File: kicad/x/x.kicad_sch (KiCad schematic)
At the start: 4 parts

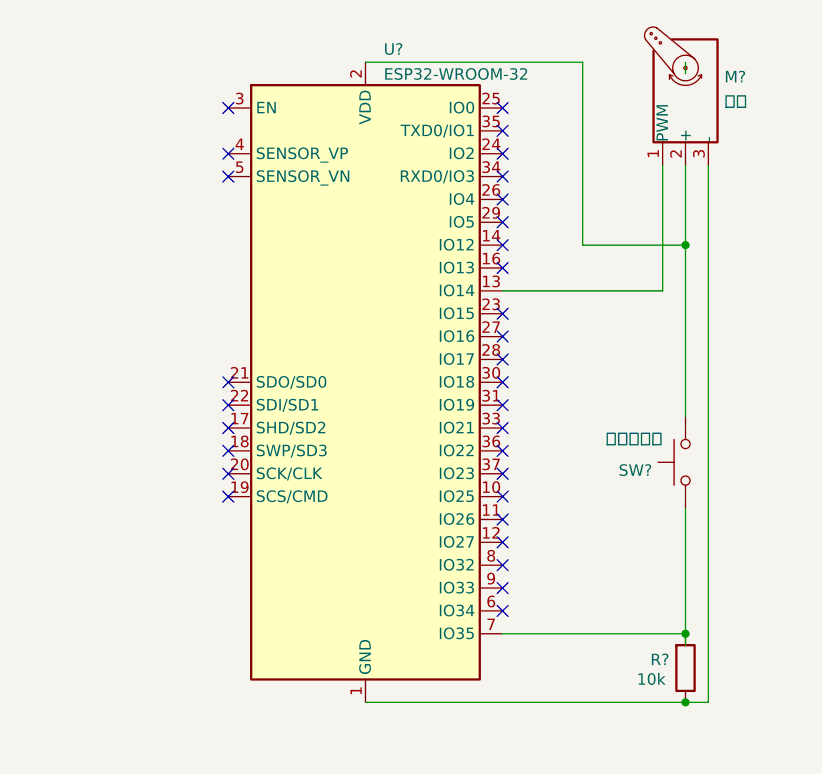
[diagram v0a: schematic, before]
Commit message: 电阻更新
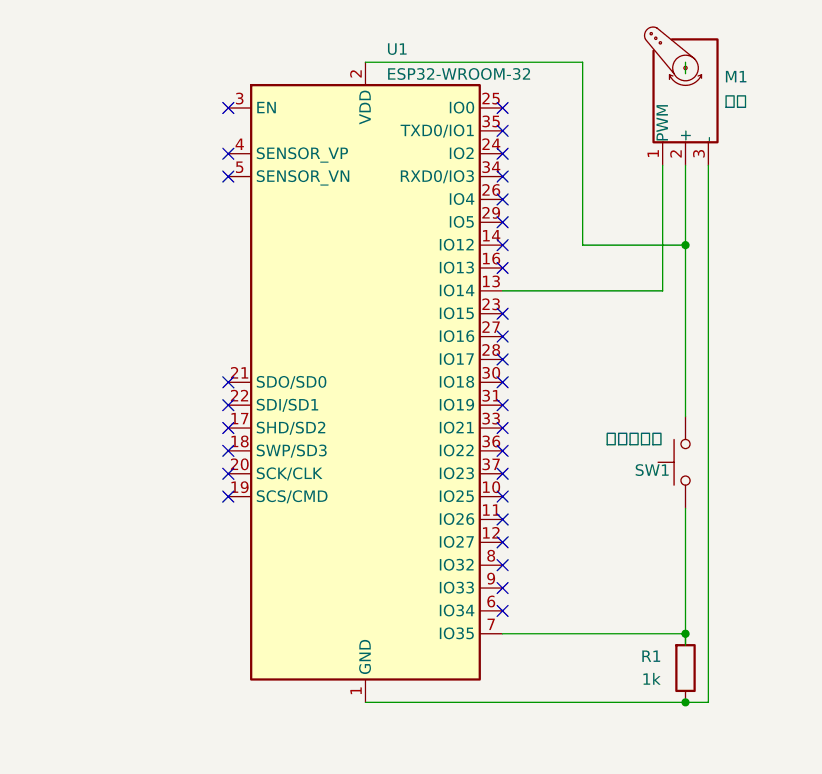
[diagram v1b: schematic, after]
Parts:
- R1: renamed from R?; value 10k -> 1k
- gave numbers to parts that had none: 3
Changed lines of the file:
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@@
   (symbol (lib_id "Motor:Motor_Servo") (at 165.1 24.13 90) (unit 1)
     (in_bom yes) (on_board yes) (fields_autoplaced)
-    (property "Reference" "M?" (id 0) (at 169.418 21.9626 90)
+    (property "Reference" "M1" (id 0) (at 169.418 21.9626 90)
       (effects (font (size 1.27 1.27)) (justify right))
     )
@@
   (symbol (lib_id "RF_Module:ESP32-WROOM-32") (at 129.54 55.88 0) (unit 1)
     (in_bom yes) (on_board yes) (fields_autoplaced)
-    (property "Reference" "U?" (id 0) (at 131.5594 18.8935 0)
+    (property "Reference" "U1" (id 0) (at 131.8832 18.8935 0)
       (effects (font (size 1.27 1.27)) (justify left))
     )
-    (property "Value" "ESP32-WROOM-32" (id 1) (at 131.5594 21.6686 0)
+    (property "Value" "ESP32-WROOM-32" (id 1) (at 131.8832 21.6686 0)
       (effects (font (size 1.27 1.27)) (justify left))
     )
@@
   (symbol (lib_id "Device:R") (at 165.1 87.63 0) (mirror x) (unit 1)
     (in_bom yes) (on_board yes)
-    (property "Reference" "R?" (id 0) (at 163.322 86.7215 0)
-      (effects (font (size 1.27 1.27)) (justify right))
-    )
-    (property "Value" "10k" (id 1) (at 161.29 88.9 0))
+    (property "Reference" "R1" (id 0) (at 161.29 86.36 0))
+    (property "Value" "1k" (id 1) (at 161.29 88.9 0))
     (property "Footprint" "" (id 2) (at 163.322 87.63 90)
       (effects (font (size 1.27 1.27)) hide)
@@
   (symbol (lib_id "Switch:SW_Push") (at 165.1 64.77 90) (unit 1)
     (in_bom yes) (on_board yes)
-    (property "Reference" "SW?" (id 0) (at 161.417 65.6785 90)
-      (effects (font (size 1.27 1.27)) (justify left))
-    )
+    (property "Reference" "SW1" (id 0) (at 161.417 65.6785 90))
     (property "Value" "雨滴传感器" (id 1) (at 162.56 62.23 90)
       (effects (font (size 1.27 1.27)) (justify left))
@@
   (symbol_instances
     (path "/3198b8ca-7d11-4e0c-89a4-c173f9fcf724"
-      (reference "M?") (unit 1) (value "舵机") (footprint "")
+      (reference "M1") (unit 1) (value "舵机") (footprint "")
     )
     (path "/bbf4e6eb-a71b-4f11-8567-3dcd30e29c2b"
-      (reference "R?") (unit 1) (value "10k") (footprint "")
+      (reference "R1") (unit 1) (value "1k") (footprint "")
     )
     (path "/d66aba20-f622-459e-9501-d2e31955a3ae"
-      (reference "SW?") (unit 1) (value "雨滴传感器") (footprint "")
+      (reference "SW1") (unit 1) (value "雨滴传感器") (footprint "")
     )
     (path "/87c4c6cd-a743-45fa-8a20-56ccd5bd596e"
-      (reference "U?") (unit 1) (value "ESP32-WROOM-32") (footprint "RF_Module:ESP32-WROOM-32")
+      (reference "U1") (unit 1) (value "ESP32-WROOM-32") (footprint "RF_Module:ESP32-WROOM-32")
     )
   )

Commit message: 增加电源
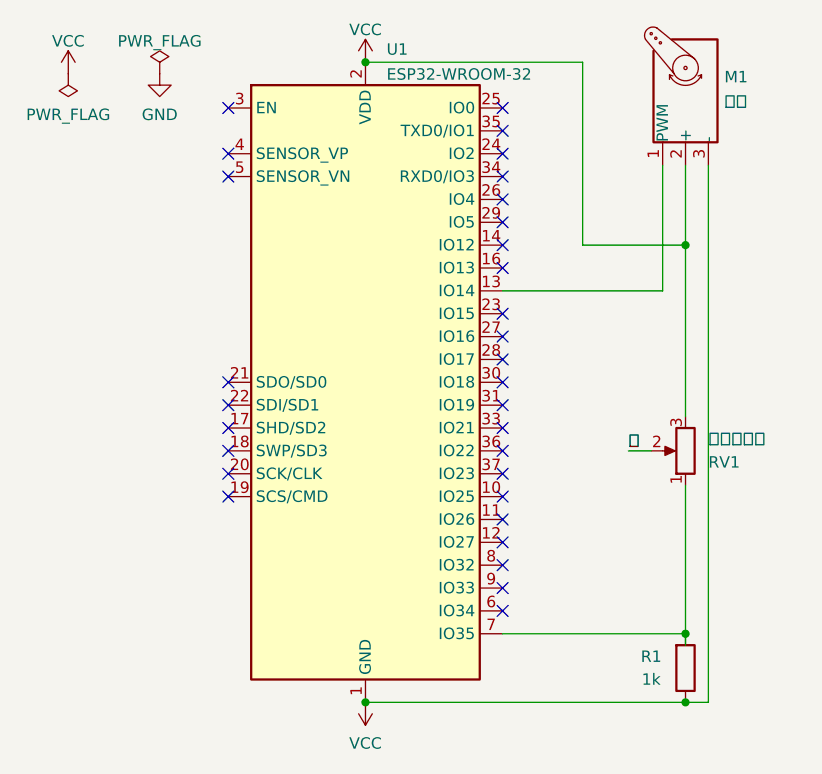
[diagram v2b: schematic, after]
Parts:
- removed SW1: 雨滴传感器, symbol Switch:SW_Push
- added RV1: 雨滴传感器, symbol Device:R_Potentiometer
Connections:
- net VCC: now reaches M1.2 (+), U1.2 (VDD)
- net VCC: now also M1.3 (-), R1.1, U1.1 (GND), U1.15 (GND), U1.38 (GND), U1.39 (GND), RV1.3
- net at R1.2, U1.7 (IO35): now also RV1.1
- new net 水: RV1.2
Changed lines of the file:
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@@
   (junction (at 165.1 91.44) (diameter 0) (color 0 0 0 0)
   )
+  (junction (at 129.54 20.32) (diameter 0) (color 0 0 0 0)
+  )
   (junction (at 165.1 83.82) (diameter 0) (color 0 0 0 0)
+  )
+  (junction (at 129.54 91.44) (diameter 0) (color 0 0 0 0)
   )
   (junction (at 165.1 40.64) (diameter 0) (color 0 0 0 0)
@@
     (stroke (width 0) (type default))
   )
-  (wire (pts (xy 165.1 21.59) (xy 165.1 20.32))
-    (stroke (width 0) (type default))
-  )
-  (wire (pts (xy 165.1 69.85) (xy 165.1 83.82))
+  (wire (pts (xy 158.75 63.5) (xy 161.29 63.5))
+    (stroke (width 0) (type default))
+  )
+  (wire (pts (xy 165.1 67.31) (xy 165.1 83.82))
     (stroke (width 0) (type default))
   )
@@
   (wire (pts (xy 153.67 40.64) (xy 153.67 20.32))
     (stroke (width 0) (type default))
+  )
+  (label "水" (at 158.75 63.5 0) (fields_autoplaced)
+    (effects (font (size 1.27 1.27)) (justify left bottom))
+  )
+  (symbol (lib_id "power:GND") (at 106.68 21.59 0) (unit 1)
+    (in_bom yes) (on_board yes) (fields_autoplaced)
+    (property "Reference" "#PWR0103" (id 0) (at 106.68 27.94 0)
+      (effects (font (size 1.27 1.27)) hide)
+    )
+    (property "Value" "GND" (id 1) (at 106.68 26.1525 0))
+    (property "Footprint" "" (id 2) (at 106.68 21.59 0)
+      (effects (font (size 1.27 1.27)) hide)
+    )
+    (property "Datasheet" "" (id 3) (at 106.68 21.59 0)
+      (effects (font (size 1.27 1.27)) hide)
+    )
+    (pin "1")
+  )
+  (symbol (lib_id "power:VCC") (at 129.54 91.44 180) (unit 1)
+    (in_bom yes) (on_board yes) (fields_autoplaced)
+    (property "Reference" "#PWR0104" (id 0) (at 129.54 87.63 0)
+      (effects (font (size 1.27 1.27)) hide)
+    )
+    (property "Value" "VCC" (id 1) (at 129.54 96.0025 0))
+    (property "Footprint" "" (id 2) (at 129.54 91.44 0)
+      (effects (font (size 1.27 1.27)) hide)
+    )
+    (property "Datasheet" "" (id 3) (at 129.54 91.44 0)
+      (effects (font (size 1.27 1.27)) hide)
+    )
+    (pin "1")
+  )
+  (symbol (lib_id "power:PWR_FLAG") (at 96.52 21.59 180) (unit 1)
+    (in_bom yes) (on_board yes) (fields_autoplaced)
+    (property "Reference" "#FLG0102" (id 0) (at 96.52 23.495 0)
+      (effects (font (size 1.27 1.27)) hide)
+    )
+    (property "Value" "PWR_FLAG" (id 1) (at 96.52 26.1525 0))
+    (property "Footprint" "" (id 2) (at 96.52 21.59 0)
+      (effects (font (size 1.27 1.27)) hide)
+    )
+    (property "Datasheet" "~" (id 3) (at 96.52 21.59 0)
+      (effects (font (size 1.27 1.27)) hide)
+    )
+    (pin "1")
   )
   (symbol (lib_id "Motor:Motor_Servo") (at 165.1 24.13 90) (unit 1)
@@
     (pin "2")
     (pin "3")
+  )
+  (symbol (lib_id "power:VCC") (at 96.52 21.59 0) (unit 1)
+    (in_bom yes) (on_board yes) (fields_autoplaced)
+    (property "Reference" "#PWR0102" (id 0) (at 96.52 25.4 0)
+      (effects (font (size 1.27 1.27)) hide)
+    )
+    (property "Value" "VCC" (id 1) (at 96.52 17.9855 0))
+    (property "Footprint" "" (id 2) (at 96.52 21.59 0)
+      (effects (font (size 1.27 1.27)) hide)
+    )
+    (property "Datasheet" "" (id 3) (at 96.52 21.59 0)
+      (effects (font (size 1.27 1.27)) hide)
+    )
+    (pin "1")
+  )
+  (symbol (lib_id "power:VCC") (at 129.54 20.32 0) (unit 1)
+    (in_bom yes) (on_board yes) (fields_autoplaced)
+    (property "Reference" "#PWR0101" (id 0) (at 129.54 24.13 0)
+      (effects (font (size 1.27 1.27)) hide)
+    )
+    (property "Value" "VCC" (id 1) (at 129.54 16.7155 0))
+    (property "Footprint" "" (id 2) (at 129.54 20.32 0)
+      (effects (font (size 1.27 1.27)) hide)
+    )
+    (property "Datasheet" "" (id 3) (at 129.54 20.32 0)
+      (effects (font (size 1.27 1.27)) hide)
+    )
+    (pin "1")
   )
   (symbol (lib_id "RF_Module:ESP32-WROOM-32") (at 129.54 55.88 0) (unit 1)
@@
     (pin "9")
   )
+  (symbol (lib_id "power:PWR_FLAG") (at 106.68 21.59 0) (unit 1)
+    (in_bom yes) (on_board yes) (fields_autoplaced)
+    (property "Reference" "#FLG0101" (id 0) (at 106.68 19.685 0)
+      (effects (font (size 1.27 1.27)) hide)
+    )
+    (property "Value" "PWR_FLAG" (id 1) (at 106.68 17.9855 0))
+    (property "Footprint" "" (id 2) (at 106.68 21.59 0)
+      (effects (font (size 1.27 1.27)) hide)
+    )
+    (property "Datasheet" "~" (id 3) (at 106.68 21.59 0)
+      (effects (font (size 1.27 1.27)) hide)
+    )
+    (pin "1")
+  )
   (symbol (lib_id "Device:R") (at 165.1 87.63 0) (mirror x) (unit 1)
     (in_bom yes) (on_board yes)
@@
     (pin "2")
   )
-  (symbol (lib_id "Switch:SW_Push") (at 165.1 64.77 90) (unit 1)
+  (symbol (lib_id "Device:R_Potentiometer") (at 165.1 63.5 180) (unit 1)
     (in_bom yes) (on_board yes)
-    (property "Reference" "SW1" (id 0) (at 161.417 65.6785 90))
-    (property "Value" "雨滴传感器" (id 1) (at 162.56 62.23 90)
-      (effects (font (size 1.27 1.27)) (justify left))
-    )
-    (property "Footprint" "" (id 2) (at 160.02 64.77 0)
-      (effects (font (size 1.27 1.27)) hide)
-    )
-    (property "Datasheet" "~" (id 3) (at 160.02 64.77 0)
+    (property "Reference" "RV1" (id 0) (at 167.64 64.77 0)
+      (effects (font (size 1.27 1.27)) (justify right))
+    )
+    (property "Value" "雨滴传感器" (id 1) (at 167.64 62.23 0)
+      (effects (font (size 1.27 1.27)) (justify right))
+    )
+    (property "Footprint" "" (id 2) (at 165.1 63.5 0)
+      (effects (font (size 1.27 1.27)) hide)
+    )
+    (property "Datasheet" "~" (id 3) (at 165.1 63.5 0)
       (effects (font (size 1.27 1.27)) hide)
     )
     (pin "1")
     (pin "2")
+    (pin "3")
   )
   (sheet_instances
@@
   )
   (symbol_instances
+    (path "/9888ccfe-5c4c-47f1-9166-d9f5b3ea6045"
+      (reference "#FLG0101") (unit 1) (value "PWR_FLAG") (footprint "")
+    )
+    (path "/2bbafe1b-5010-4cc4-97c4-31d1f969cd08"
+      (reference "#FLG0102") (unit 1) (value "PWR_FLAG") (footprint "")
+    )
+    (path "/86f6faec-7eee-404c-a73a-2ae625f33d8c"
+      (reference "#PWR0101") (unit 1) (value "VCC") (footprint "")
+    )
+    (path "/7a0dea2f-98b5-4afe-8d5d-f39ea5db6892"
+      (reference "#PWR0102") (unit 1) (value "VCC") (footprint "")
+    )
+    (path "/0e31ffcf-99fb-4275-800d-d27579fe3735"
+      (reference "#PWR0103") (unit 1) (value "GND") (footprint "")
+    )
+    (path "/102e44d6-9086-4c43-bf41-0a02d894bf05"
+      (reference "#PWR0104") (unit 1) (value "VCC") (footprint "")
+    )
     (path "/3198b8ca-7d11-4e0c-89a4-c173f9fcf724"
       (reference "M1") (unit 1) (value "舵机") (footprint "")
@@
       (reference "R1") (unit 1) (value "1k") (footprint "")
     )
-    (path "/d66aba20-f622-459e-9501-d2e31955a3ae"
-      (reference "SW1") (unit 1) (value "雨滴传感器") (footprint "")
+    (path "/e5a837b5-132c-4613-a340-a2044777a4a1"
+      (reference "RV1") (unit 1) (value "雨滴传感器") (footprint "")
     )
     (path "/87c4c6cd-a743-45fa-8a20-56ccd5bd596e"
